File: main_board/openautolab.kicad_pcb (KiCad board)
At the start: 2 copper layers, 109.2 x 74.9 mm, 30 parts, among them IC1 ULN2065B, IC3 ULN2065B, J1 PIN8, J10 FILTER_PUMP, J11 FILTER_SENSOR, J12 PWR_IN, J13 HX711, J14 SERVO, J15 LCD, J2 PIN9, J3 PIN10, J4 PIN11, J5 PIN7, J6 PIN6, J7 PIN5, J8 PINA0, J9 PUMP, SW0 PIN_A3, SW1 PIN_A2, SW2 PIN_A1, SW3 SW_DPST_x2, SW4 SW_DPST_x2, U2 LM2575-5.0BT

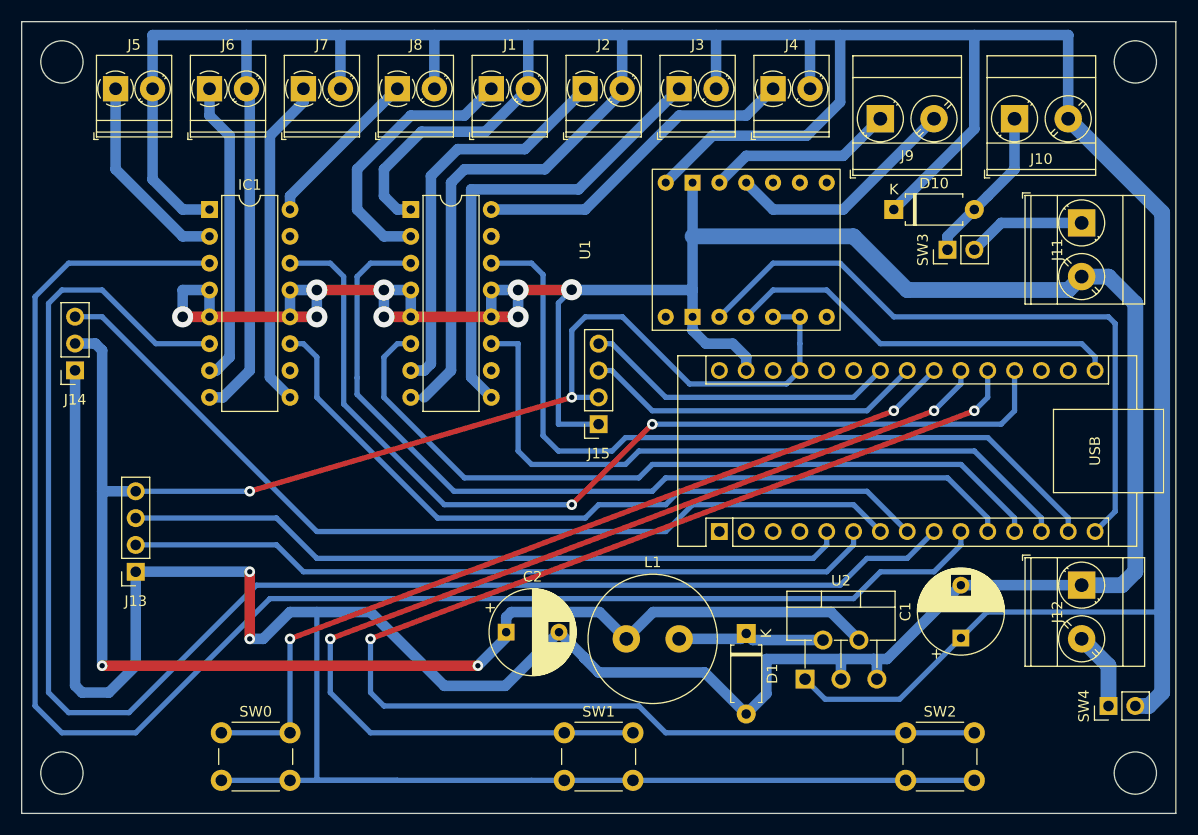
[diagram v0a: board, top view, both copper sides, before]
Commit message: add ground plane
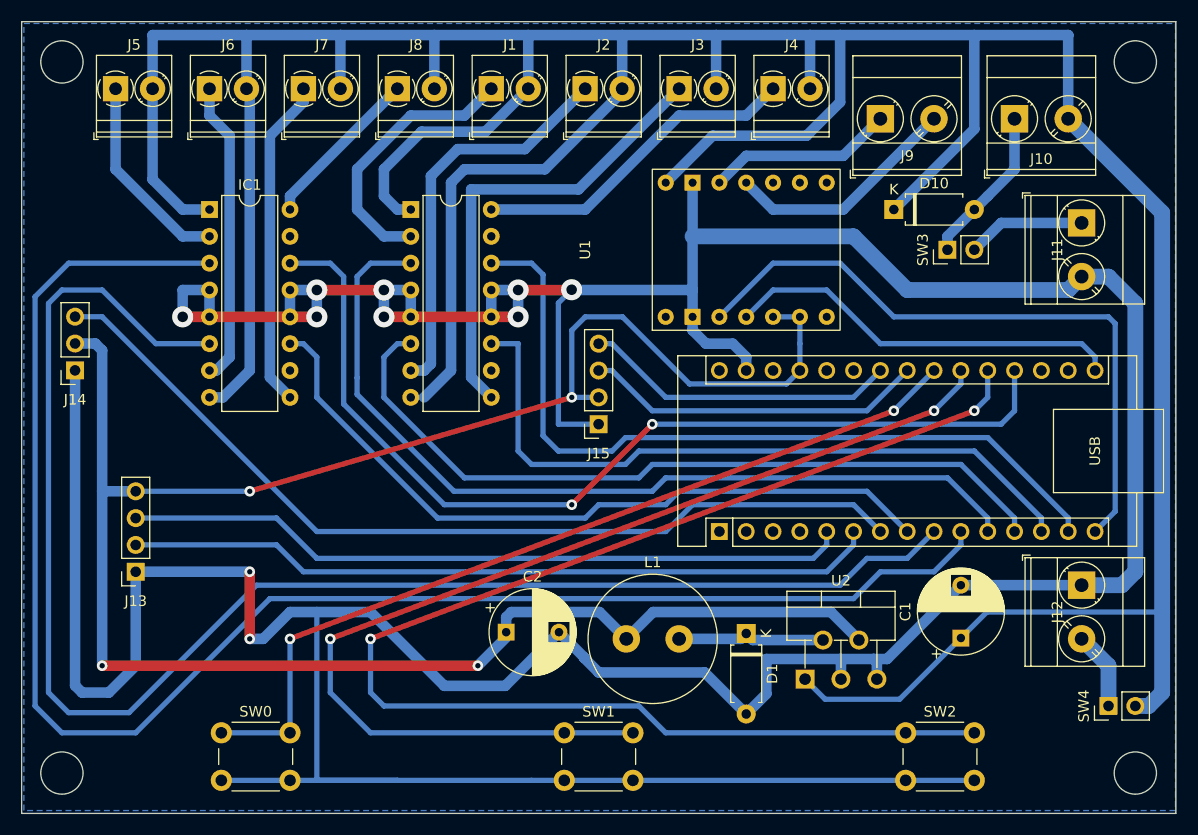
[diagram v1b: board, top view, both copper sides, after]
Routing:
- added copper zone on B.Cu, net GND

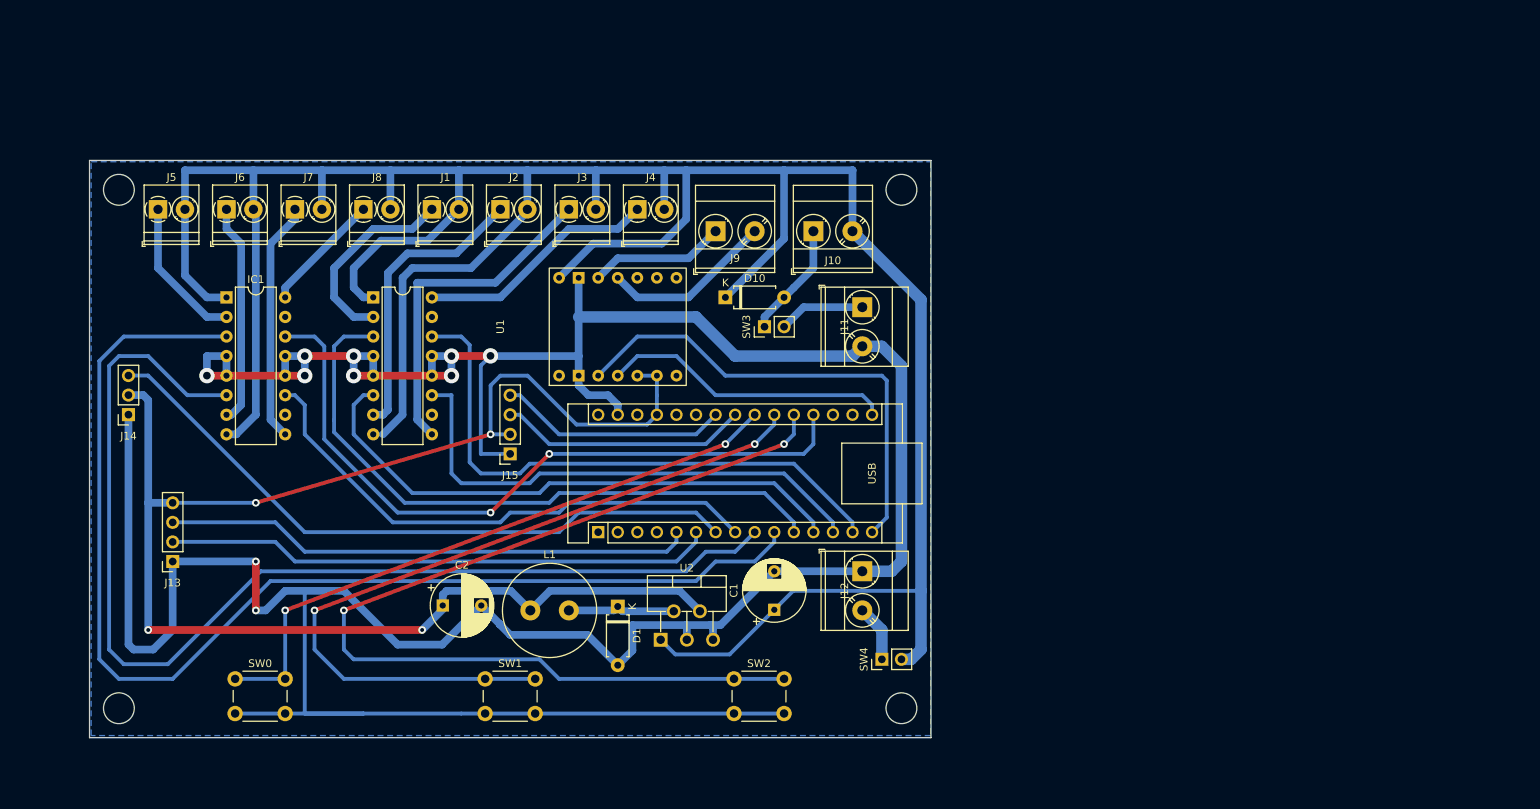
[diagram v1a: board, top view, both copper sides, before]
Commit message: update schematic
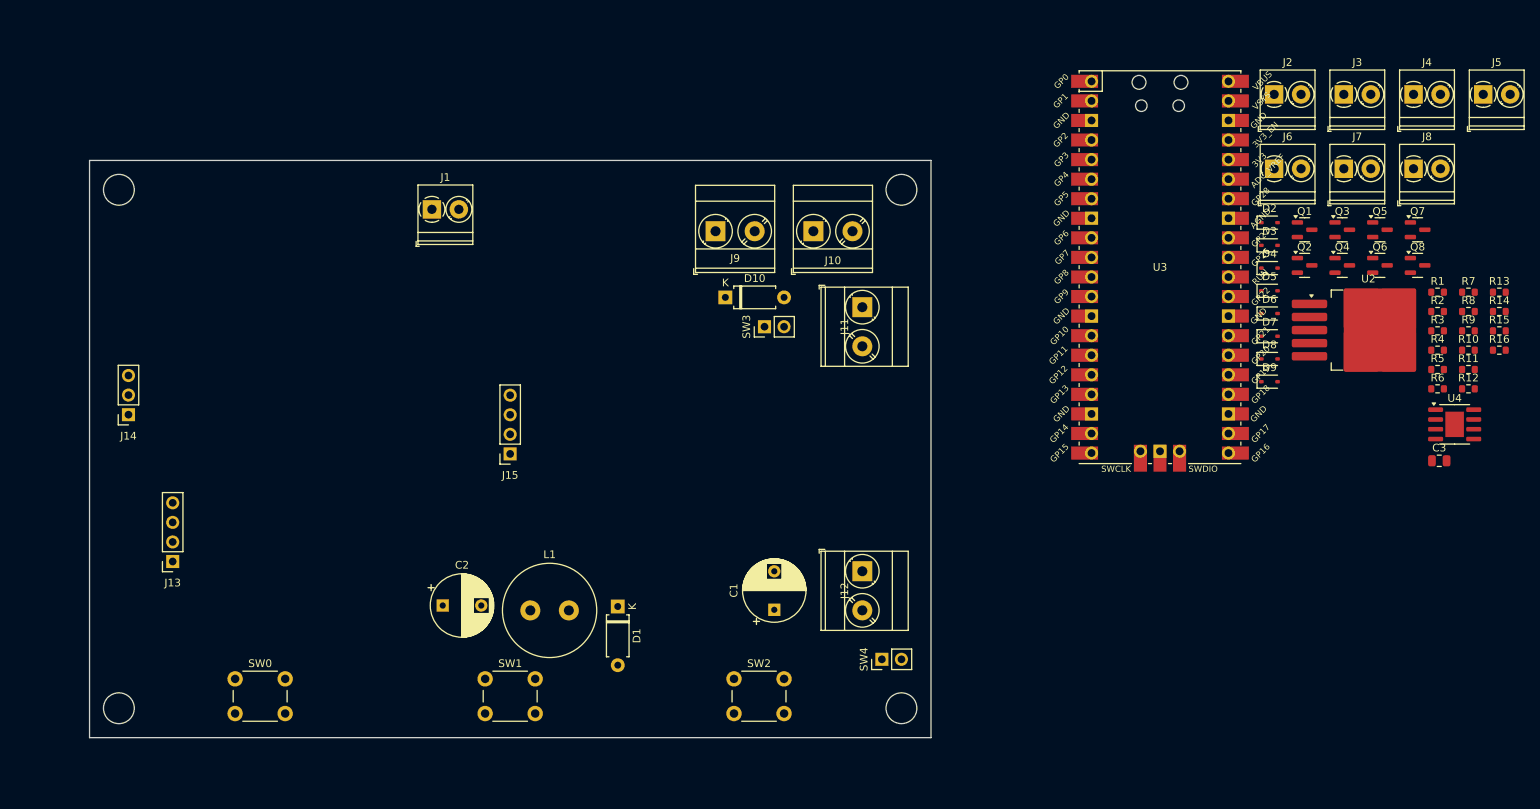
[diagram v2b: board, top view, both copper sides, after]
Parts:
- removed A1: Arduino_Nano_v3.x, Module:Arduino_Nano
- removed IC1, IC3: ULN2065B, Package_DIP:DIP-16_W7.62mm
- removed U1: ~, Pololu_breakout_DRV8874:Pololu_breakout_DRV8874
- added C3: 220nf, Capacitor_SMD:C_0805_2012Metric, F.Cu at (209.5, 75.8)
- added D2: 1N5819WS, Diode_SMD:D_SOD-323, F.Cu at (187.5, 44.9)
- added D3: 1N5819WS, Diode_SMD:D_SOD-323, F.Cu at (187.5, 47.9)
- added D4: 1N5819WS, Diode_SMD:D_SOD-323, F.Cu at (187.5, 50.8)
- added D5: 1N5819WS, Diode_SMD:D_SOD-323, F.Cu at (187.5, 53.8)
- added D6: 1N5819WS, Diode_SMD:D_SOD-323, F.Cu at (187.5, 56.7)
- added D7: 1N5819WS, Diode_SMD:D_SOD-323, F.Cu at (187.5, 59.7)
- added D8: 1N5819WS, Diode_SMD:D_SOD-323, F.Cu at (187.5, 62.6)
- added D9: 1N5819WS, Diode_SMD:D_SOD-323, F.Cu at (187.5, 65.6)
- added Q1: TSM2302CX, Package_TO_SOT_SMD:SOT-23, F.Cu at (192.0, 45.8)
- added Q2: TSM2302CX, Package_TO_SOT_SMD:SOT-23, F.Cu at (192.0, 50.5)
- added Q3: TSM2302CX, Package_TO_SOT_SMD:SOT-23, F.Cu at (196.9, 45.8)
- added Q4: TSM2302CX, Package_TO_SOT_SMD:SOT-23, F.Cu at (196.9, 50.5)
- added Q5: TSM2302CX, Package_TO_SOT_SMD:SOT-23, F.Cu at (201.8, 45.8)
- added Q6: TSM2302CX, Package_TO_SOT_SMD:SOT-23, F.Cu at (201.8, 50.5)
- added Q7: TSM2302CX, Package_TO_SOT_SMD:SOT-23, F.Cu at (206.7, 45.8)
- added Q8: TSM2302CX, Package_TO_SOT_SMD:SOT-23, F.Cu at (206.7, 50.5)
- added R1: 100, Resistor_SMD:R_0603_1608Metric, F.Cu at (209.3, 53.9)
- added R10: 10k, Resistor_SMD:R_0603_1608Metric, F.Cu at (213.3, 61.5)
- added R11: 100, Resistor_SMD:R_0603_1608Metric, F.Cu at (213.3, 64.0)
- added R12: 10k, Resistor_SMD:R_0603_1608Metric, F.Cu at (213.3, 66.5)
- added R13: 100, Resistor_SMD:R_0603_1608Metric, F.Cu at (217.3, 53.9)
- added R14: 10k, Resistor_SMD:R_0603_1608Metric, F.Cu at (217.3, 56.4)
- added R15: 100, Resistor_SMD:R_0603_1608Metric, F.Cu at (217.3, 59.0)
- added R16: 10k, Resistor_SMD:R_0603_1608Metric, F.Cu at (217.3, 61.5)
- added R2: 10k, Resistor_SMD:R_0603_1608Metric, F.Cu at (209.3, 56.4)
- added R3: 100, Resistor_SMD:R_0603_1608Metric, F.Cu at (209.3, 59.0)
- added R4: 10k, Resistor_SMD:R_0603_1608Metric, F.Cu at (209.3, 61.5)
- added R5: 100, Resistor_SMD:R_0603_1608Metric, F.Cu at (209.3, 64.0)
- added R6: 10k, Resistor_SMD:R_0603_1608Metric, F.Cu at (209.3, 66.5)
- added R7: 100, Resistor_SMD:R_0603_1608Metric, F.Cu at (213.3, 53.9)
- added R8: 10k, Resistor_SMD:R_0603_1608Metric, F.Cu at (213.3, 56.4)
- added R9: 100, Resistor_SMD:R_0603_1608Metric, F.Cu at (213.3, 59.0)
- added U3: Pico, dev:RPi_Pico_SMD_TH, F.Cu at (173.3, 50.7)
- added U4: A4950E, Package_SO:SOIC-8-1EP_3.9x4.9mm_P1.27mm_EP2.41x3.3mm, F.Cu at (211.5, 71.1)
- J1: value PIN8 -> GP7
- J15: value LCD -> Display
- J2: value PIN9 -> GP6
- J3: value PIN10 -> GP5
- J4: value PIN11 -> GP4
- J5: value PIN7 -> GP3
- J6: value PIN6 -> GP2
- J7: value PIN5 -> GP1
- J8: value PINA0 -> GP0
- SW0: value PIN_A3 -> GP20
- SW1: value PIN_A2 -> GP21
- SW2: value PIN_A1 -> GP22
- U2: footprint Package_TO_SOT_THT:TO-220-5_P3.4x3.7mm_StaggerOdd_Lead3.8mm_Vertical -> Package_TO_SOT_SMD:TO-263-5_TabPin3
- moved J5 172.7 mm to (215.2, 28.3)
- moved J8 136.4 mm to (206.2, 37.9)
- moved J7 136.3 mm to (197.1, 37.9)
- moved J6 136.1 mm to (188.1, 37.9)
- moved J4 101.9 mm to (206.2, 28.3)
- moved J3 101.7 mm to (197.1, 28.3)
- moved J2 101.6 mm to (188.1, 28.3)
- moved U2 100.3 mm to (200.3, 58.9)
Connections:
- J1 pad 1: Net-(IC3-O1) -> +12V
- J1 pad 2: +12V -> Net-(D2-A)
- J2 pad 1: Net-(IC3-O2) -> +12V
- J2 pad 2: +12V -> Net-(D3-A)
- J3 pad 1: Net-(IC3-O3) -> +12V
- J3 pad 2: +12V -> Net-(D4-A)
- J4 pad 1: Net-(IC3-O4) -> +12V
- J4 pad 2: +12V -> Net-(D5-A)
- J5 pad 1: Net-(IC1-O1) -> +12V
- J5 pad 2: +12V -> Net-(D6-A)
- J6 pad 1: Net-(IC1-O2) -> +12V
- J6 pad 2: +12V -> Net-(D7-A)
- J7 pad 1: Net-(IC1-O3) -> +12V
- J7 pad 2: +12V -> Net-(D8-A)
- J8 pad 1: Net-(IC1-O4) -> +12V
- J8 pad 2: +12V -> Net-(D9-A)
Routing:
- net GND: track 450.5 -> 0.00 mm, vias 10 -> 0
- net +12V: track 391.9 -> 0.00 mm
- net +5V: track 198.2 -> 0.00 mm, vias 4 -> 0
- net Net-(A1-D7): track 153.9 -> 0.00 mm
- net Net-(A1-D6): track 146.4 -> 0.00 mm
- net Net-(U3-GPIO22): track 129.2 -> 0.00 mm, vias 2 -> 0
- net Net-(U3-GPIO21): track 101.3 -> 0.00 mm, vias 2 -> 0
- net Net-(A1-A0): track 92.6 -> 0.00 mm, vias 2 -> 0
- net Net-(J14-Pin_3): track 86.8 -> 0.00 mm
- net Net-(A1-D8): track 83.6 -> 0.00 mm
- net Net-(U3-GPIO20): track 81.9 -> 0.00 mm, vias 2 -> 0
- net Net-(A1-D11): track 75.9 -> 0.00 mm
- net Net-(A1-D9): track 73.6 -> 0.00 mm
- net Net-(J13-Pin_2): track 71.3 -> 0.00 mm
- net Net-(A1-D5): track 70.1 -> 0.00 mm
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- removed copper zone on B.Cu, net GND

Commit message: all footprints correct except toggle switch
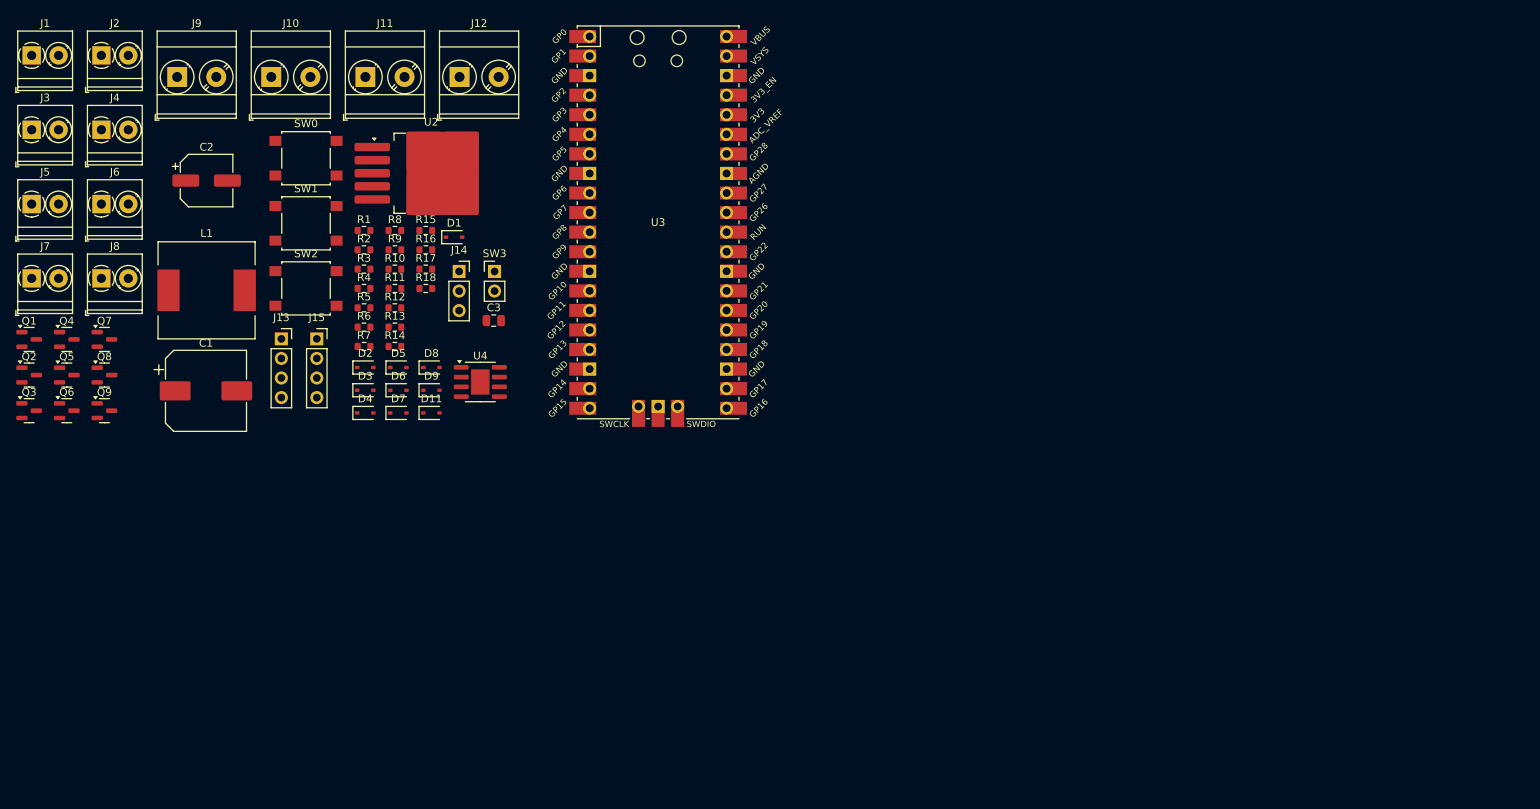
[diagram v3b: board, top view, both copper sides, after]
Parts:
- removed D10: 1N5819WS, Diode_THT:D_A-405_P7.62mm_Horizontal
- removed SW4: SW_DPST_x2, Connector_PinHeader_2.54mm:PinHeader_1x02_P2.54mm_Vertical
- added D11: 1N5819WS, Diode_SMD:D_SOD-323, F.Cu at (78.7, 69.6)
- added Q9: TSM2302CX, Package_TO_SOT_SMD:SOT-23, F.Cu at (36.2, 69.3)
- added R17: 100, Resistor_SMD:R_0603_1608Metric, F.Cu at (77.9, 50.9)
- added R18: 10k, Resistor_SMD:R_0603_1608Metric, F.Cu at (77.9, 53.5)
- C1: value 100 -> 200; footprint Capacitor_THT:CP_Radial_D8.0mm_P5.00mm -> Capacitor_SMD:CP_Elec_10x10
- C2: footprint Capacitor_THT:CP_Radial_D8.0mm_P5.00mm -> Capacitor_SMD:CP_Elec_6.3x7.7
- D1: footprint Diode_THT:D_A-405_P7.62mm_Horizontal -> Diode_SMD:D_SOD-323
- L1: footprint Inductor_THT:L_Radial_D12.0mm_P5.00mm_Fastron_11P -> Inductor_SMD:L_12x12mm_H8mm
- SW0, SW1, SW2: footprint Button_Switch_THT:SW_PUSH_6mm -> Button_Switch_SMD:SW_SPST_B3S-1000
- U3: footprint dev:RPi_Pico_SMD_TH -> RP-Pico:RPi_Pico_SMD_TH
- moved J5 189.0 mm to (26.8, 42.5)
- moved Q3 172.1 mm to (26.4, 69.3)
- moved Q5 171.5 mm to (31.3, 64.7)
- moved Q6 171.5 mm to (31.3, 69.3)
- moved Q7 171.1 mm to (36.2, 60.1)
- moved Q8 171.1 mm to (36.2, 64.7)
- moved J8 171.0 mm to (35.8, 52.1)
- moved J7 171.0 mm to (26.8, 52.1)
- moved J4 170.4 mm to (35.8, 32.8)
- moved J3 170.4 mm to (26.8, 32.8)
- moved Q1 166.2 mm to (26.4, 60.1)
- moved Q2 166.2 mm to (26.4, 64.7)
- moved Q4 165.9 mm to (31.3, 60.1)
- moved J2 152.3 mm to (35.8, 23.2)
- moved J6 152.3 mm to (35.8, 42.5)
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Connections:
- J10 pad 1: Net-(D10-A) -> Net-(D11-A)
- J11 pad 2: GND -> Net-(J11-Pin_2)
- J12 pad 2: Net-(J12-Pin_2) -> +12V
- SW3 pad 1: Net-(D10-A) -> Net-(J11-Pin_1)
- SW3 pad 2: Net-(J11-Pin_1) -> +5V
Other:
- board outline removed

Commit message: fix footprints
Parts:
- C1: value 200 -> 200uf
- C2: value 330 -> 330uF
- L1: value 330 -> 330uH
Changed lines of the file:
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@@
 			)
 		)
-		(property "Value" "200"
+		(property "Value" "200uf"
 			(at 0 6.2 0)
 			(layer "F.Fab")
@@
 			)
 		)
+		(property "LCSC" "C125977"
+			(at 0 0 0)
+			(layer "F.SilkS")
+			(hide yes)
+			(effects
+				(font
+					(size 1.27 1.27)
+					(thickness 0.15)
+				)
+			)
+		)
 		(property ki_fp_filters "CP_*")
 		(sheetname "Root")
@@
 			)
 		)
-		(property "Value" "330"
+		(property "Value" "330uF"
 			(at 0 4.35 0)
 			(layer "F.Fab")
@@
 			)
 		)
+		(property "LCSC" "C7471878"
+			(at 0 0 0)
+			(layer "F.SilkS")
+			(hide yes)
+			(effects
+				(font
+					(size 1.27 1.27)
+					(thickness 0.15)
+				)
+			)
+		)
 		(property ki_fp_filters "CP_*")
 		(sheetname "Root")
@@
 			)
 		)
-		(property "Value" "330"
+		(property "Value" "330uH"
 			(at 0 7.6 0)
 			(layer "F.Fab")
@@
 			)
 		)
+		(property "LCSC" "C10152"
+			(at 0 0 0)
+			(layer "F.SilkS")
+			(hide yes)
+			(effects
+				(font
+					(size 1.27 1.27)
+					(thickness 0.15)
+				)
+			)
+		)
 		(property ki_fp_filters "Choke_* *Coil* Inductor_* L_*")
 		(sheetname "Root")
@@
 			(hide yes)
 			(effects
+				(font
+					(size 1.27 1.27)
+					(thickness 0.15)
+				)
+			)
+		)
+		(property "LCSC" "C5378"
+			(at 0 0 0)
+			(layer "F.SilkS")
+			(hide yes)
+			(effects

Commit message: all footprints correct. draft of a layout
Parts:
- SW3: footprint Connector_PinHeader_2.54mm:PinHeader_1x02_P2.54mm_Vertical -> easyeda2kicad:SW-SMD_6P-L5.8-W5.8-P2.00-LS8.0_YTSPS-22E58LM
- moved Q9 96.3 mm to (130.9, 51.5)
- moved J12 92.6 mm to (129.8, 105.5), turned to -90 degrees
- moved Q6 79.3 mm to (107.9, 48.5)
- moved SW0 76.7 mm to (68.8, 113.0)
- moved SW2 74.3 mm to (106.8, 113.0)
- moved Q1 73.8 mm to (99.4, 48.5)
- moved SW1 72.6 mm to (87.8, 113.0)
- moved J14 71.8 mm to (41.8, 110.5), turned to 180 degrees
- moved J1 70.5 mm to (95.5, 38.8)
- moved J9 69.3 mm to (113.3, 41.5)
- moved J10 69.1 mm to (125.2, 41.5)
- moved J6 68.3 mm to (104.0, 38.8)
- moved J11 68.2 mm to (129.8, 59.0), turned to -90 degrees
- moved C1 67.5 mm to (116.8, 62.5), turned to 180 degrees
- moved Q2 66.4 mm to (90.9, 48.5)
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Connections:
- J10 pad 1: Net-(D11-A) -> +12V
- J10 pad 2: +12V -> Net-(D11-A)
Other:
- board outline added: 98 x 84 mm
